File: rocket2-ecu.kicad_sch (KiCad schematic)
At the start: 23 parts, among them J1 ALARM, J24 XT60, P3 PAD_SMD, P4 PAD_SMD, Q1 DMG3402L, U1 BMI088, U2 MS560702BA03-50, U3 BMM150, U4 GC-XPORT-ENH

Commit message: Finished
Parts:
- removed H4: MountingHole_Pad, MountingHole:MountingHole_4.3mm_M4_Pad_Via, symbol Mechanical:MountingHole_Pad
- added R127, R129: 15K, Resistor_SMD:R_0402_1005Metric, symbol Device:R_Small_US
- added R128, R5: 100K, Resistor_SMD:R_0402_1005Metric, symbol Device:R_Small_US
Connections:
- net GND: now also R127.2, R129.2
- net REDs/BATT_IN+ renamed BATT
- net BATT: now also R5.1
- net REDs/GSE_IN+ renamed GSE
- net GSE: now also R128.1
- new net ECU_BV: R127.1, R5.2
- new net ECU_GS: R128.2, R129.1
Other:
- note removed: "FIC GROUND VIAS AND RETURN PATHS"
- note removed: "Reads battery voltage Reads GSE voltage"

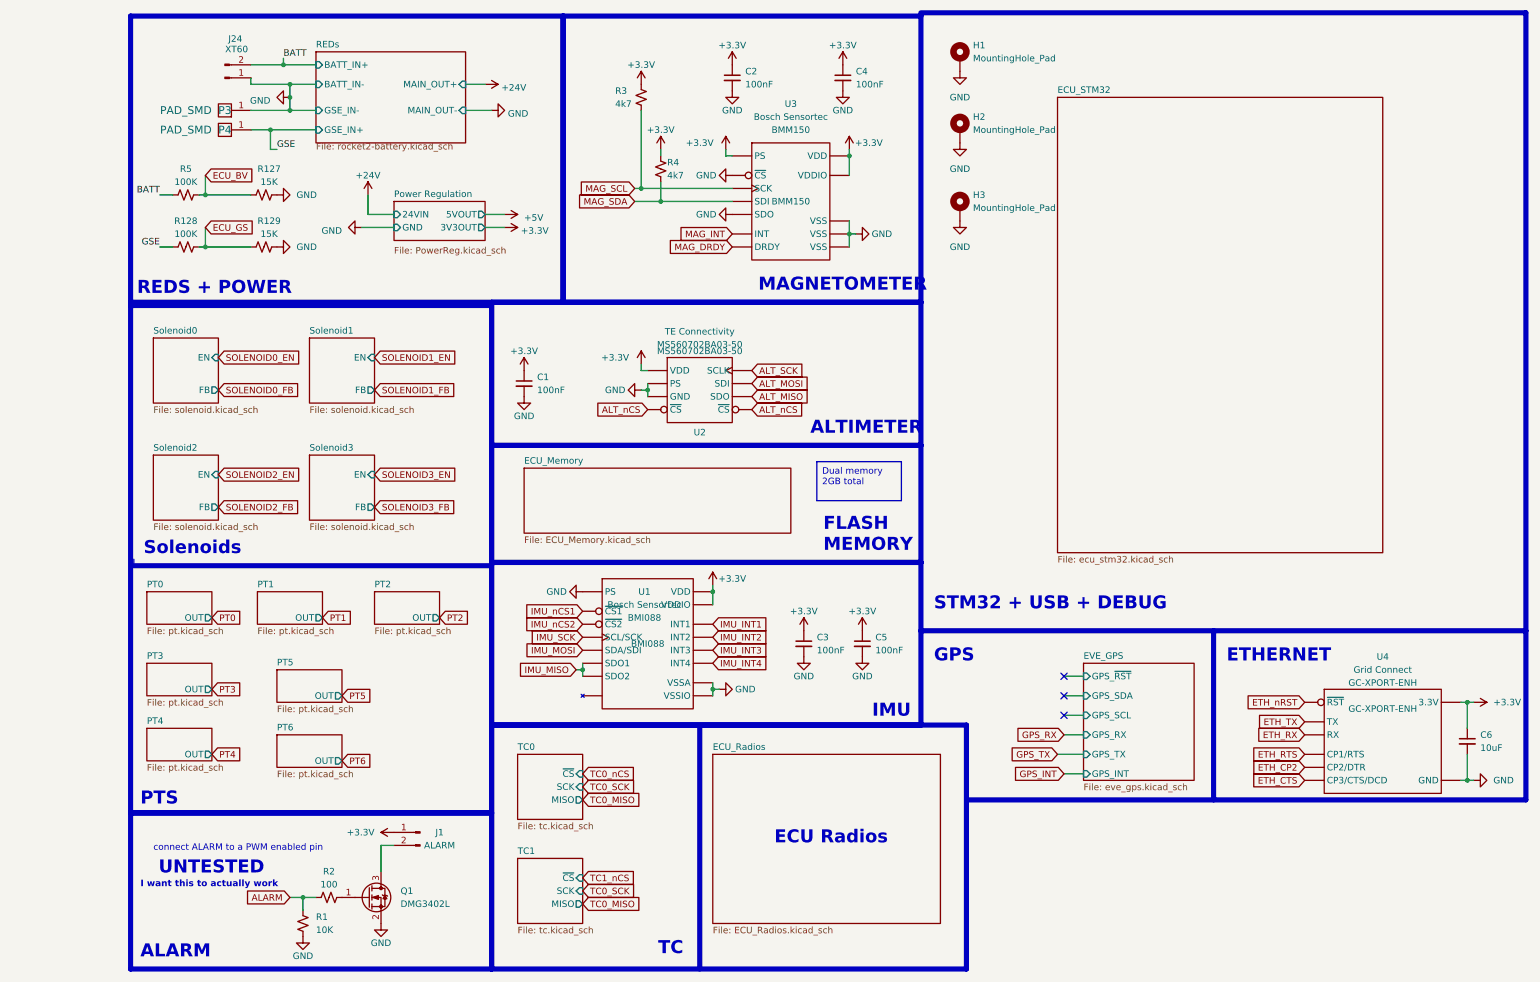
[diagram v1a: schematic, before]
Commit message: REDS updated with diodes and hierarchy to main micro
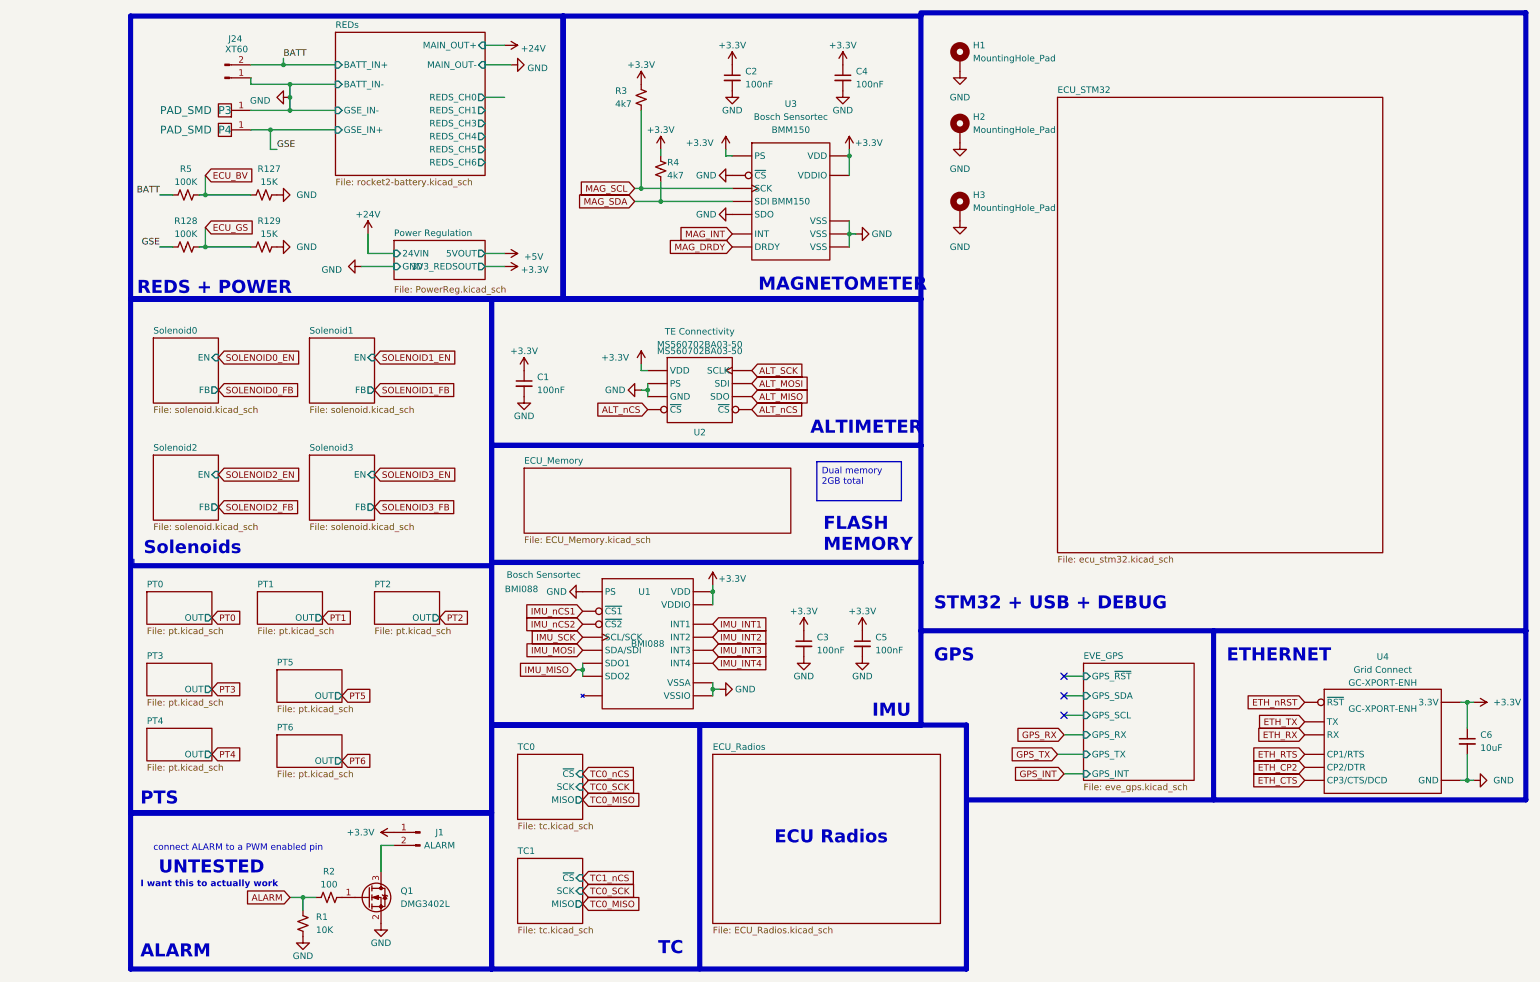
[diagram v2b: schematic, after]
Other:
- sheet Power Regulation ports: added 3V3_REDSOUT; removed 3V3OUT
- sheet REDs ports: added REDS_CH0, REDS_CH1, REDS_CH3, REDS_CH4, REDS_CH5, REDS_CH6; removed none

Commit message: Updated REDS for working
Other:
- sheet REDs ports: added REDS_CH2; removed REDS_CH6
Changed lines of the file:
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@@
 	(wire
 		(pts
+			(xy 81.28 30.48) (xy 82.55 30.48)
+		)
+		(stroke
+			(width 0)
+			(type default)
+		)
+	)
+	(wire
+		(pts
 			(xy 273.05 146.05) (xy 271.78 146.05)
 		)
@@
 	(wire
 		(pts
-			(xy 81.28 27.94) (xy 85.09 27.94)
+			(xy 81.28 27.94) (xy 82.55 27.94)
 		)
 		(stroke
@@
 	(wire
 		(pts
+			(xy 81.28 40.64) (xy 82.55 40.64)
+		)
+		(stroke
+			(width 0)
+			(type default)
+		)
+	)
+	(wire
+		(pts
+			(xy 81.28 33.02) (xy 82.55 33.02)
+		)
+		(stroke
+			(width 0)
+			(type default)
+		)
+	)
+	(wire
+		(pts
 			(xy 193.04 156.21) (xy 198.12 156.21)
 		)
@@
 	(wire
 		(pts
+			(xy 81.28 38.1) (xy 82.55 38.1)
+		)
+		(stroke
+			(width 0)
+			(type default)
+		)
+	)
+	(wire
+		(pts
 			(xy 52.07 25.4) (xy 43.18 25.4)
 		)
@@
 	(wire
 		(pts
+			(xy 81.28 35.56) (xy 82.55 35.56)
+		)
+		(stroke
+			(width 0)
+			(type default)
+		)
+	)
+	(wire
+		(pts
 			(xy 100.33 139.7) (xy 100.33 140.97)
 		)
@@
 					(size 1.27 1.27)
 				)
+				(hide yes)
 			)
 		)
@@
 			)
 		)
-		(pin "MAIN_OUT-" input
-			(at 81.28 21.59 0)
-			(effects
-				(font
-					(size 1.27 1.27)
-				)
-				(justify right)
-			)
-		)
-		(pin "MAIN_OUT+" input
-			(at 81.28 17.78 0)
-			(effects
-				(font
-					(size 1.27 1.27)
-				)
-				(justify right)
-			)
-		)
 		(pin "BATT_IN-" input
 			(at 52.07 25.4 180)
@@
 		)
 		(pin "REDS_CH4" output
-			(at 81.28 35.56 0)
+			(at 81.28 38.1 0)
 			(effects
 				(font
@@
 		)
 		(pin "REDS_CH3" output
-			(at 81.28 33.02 0)
+			(at 81.28 35.56 0)
 			(effects
 				(font
@@
 		)
 		(pin "REDS_CH5" output
-			(at 81.28 38.1 0)
+			(at 81.28 40.64 0)
 			(effects
 				(font
@@
 			)
 		)
-		(pin "REDS_CH6" output
-			(at 81.28 40.64 0)
+		(pin "REDS_CH2" output
+			(at 81.28 33.02 0)
+			(effects
+				(font
+					(size 1.27 1.27)
+				)
+				(justify right)
+			)
+		)
+		(pin "MAIN_OUT-" input
+			(at 81.28 21.59 0)
+			(effects
+				(font
+					(size 1.27 1.27)
+				)
+				(justify right)
+			)
+		)
+		(pin "MAIN_OUT+" input
+			(at 81.28 17.78 0)
 			(effects
 				(font

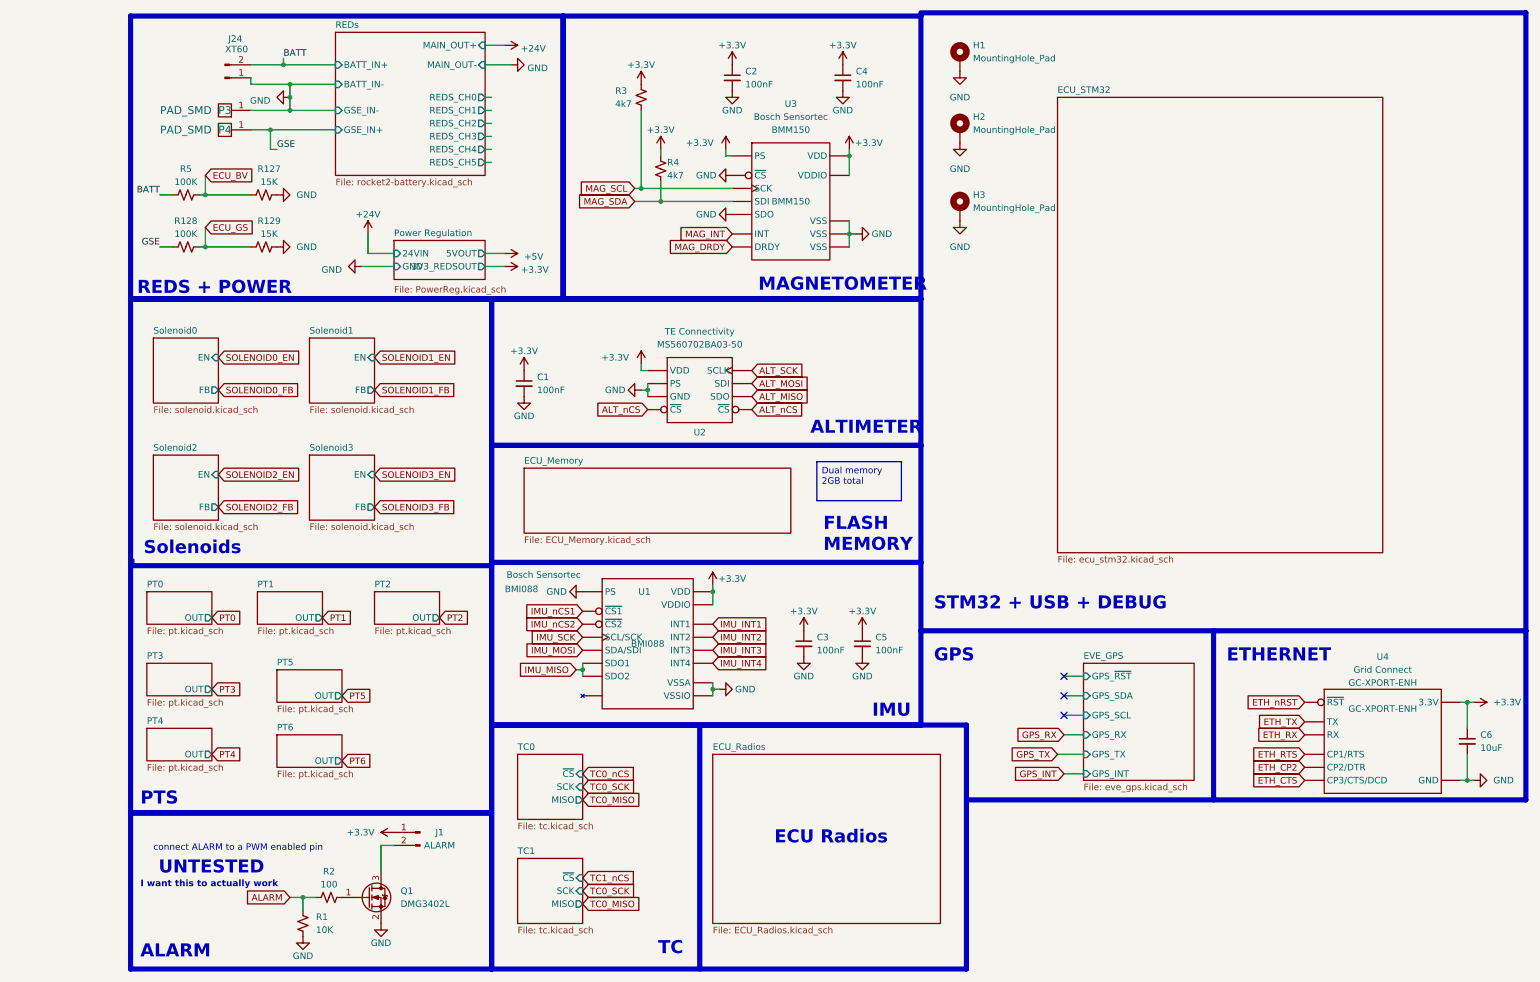
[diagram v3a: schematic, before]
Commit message: Added power sense to rocket2-battery with voltage follower, added +1 solenoids and PT circuit, made new gx connectors
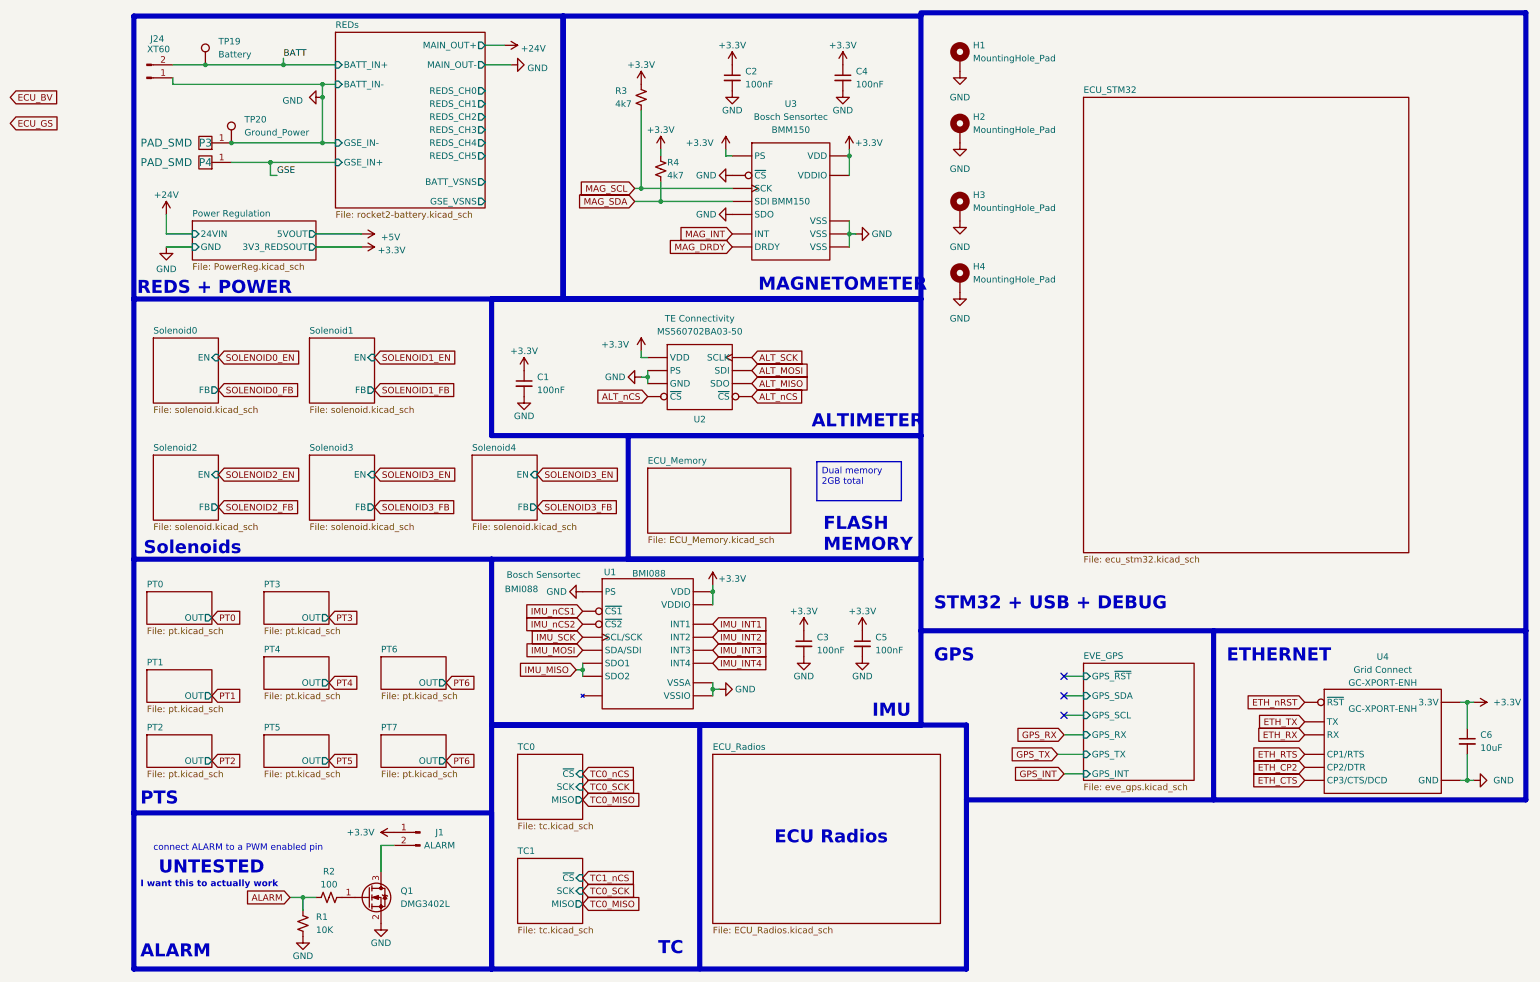
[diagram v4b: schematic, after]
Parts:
- removed R127, R129: 15K, Resistor_SMD:R_0402_1005Metric, symbol Device:R_Small_US
- removed R128, R5: 100K, Resistor_SMD:R_0402_1005Metric, symbol Device:R_Small_US
- added H4: MountingHole_Pad, MountingHole:MountingHole_4.3mm_M4_Pad_Via, symbol Mechanical:MountingHole_Pad
- added TP19: Battery, TestPoint:TestPoint_Plated_Hole_D2.0mm, symbol Connector:TestPoint
- added TP20: Ground_Power, TestPoint:TestPoint_Plated_Hole_D2.0mm, symbol Connector:TestPoint
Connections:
- net BATT: now also TP19.1
- net GND: now also H4.1, TP20.1
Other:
- added sheet PT7 (pt.kicad_sch)
- added sheet Solenoid4 (solenoid.kicad_sch)
- sheet REDs ports: added BATT_VSNS, GSE_VSNS; removed none
- moved on the sheet: J24, P3, P4, U2

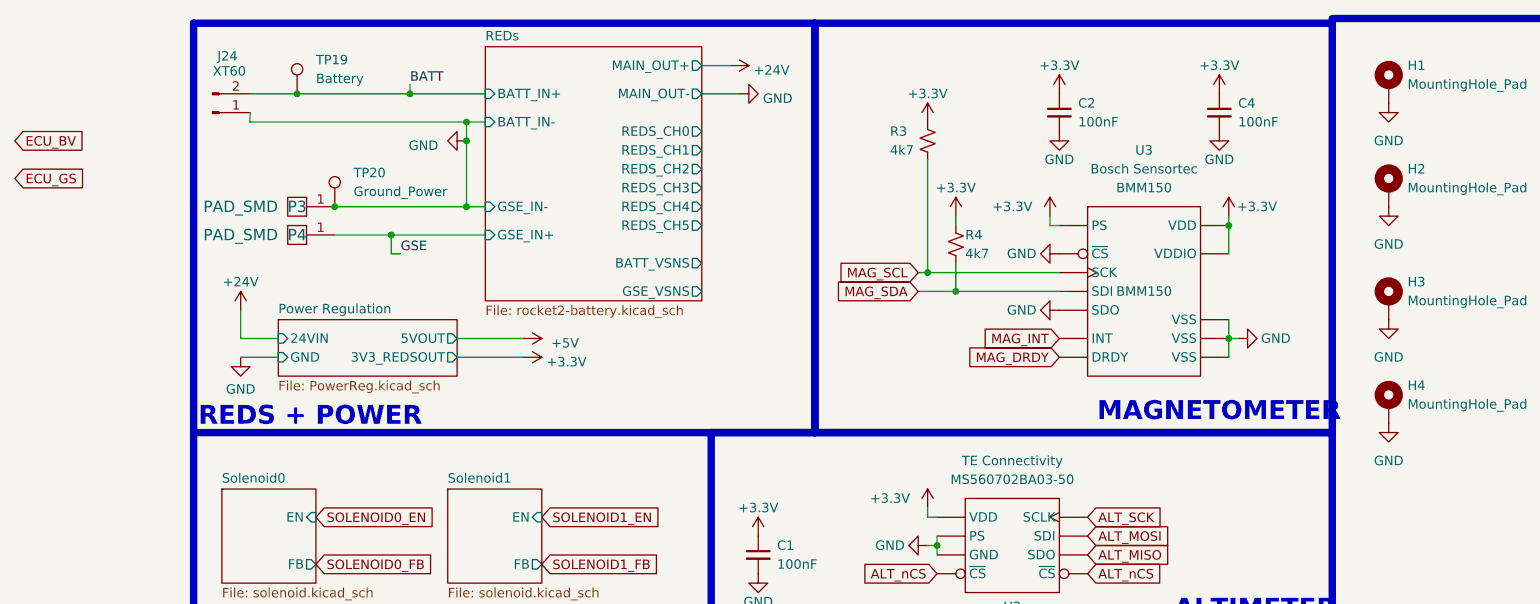
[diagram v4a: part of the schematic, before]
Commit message: moved from bmm150 to bmm350
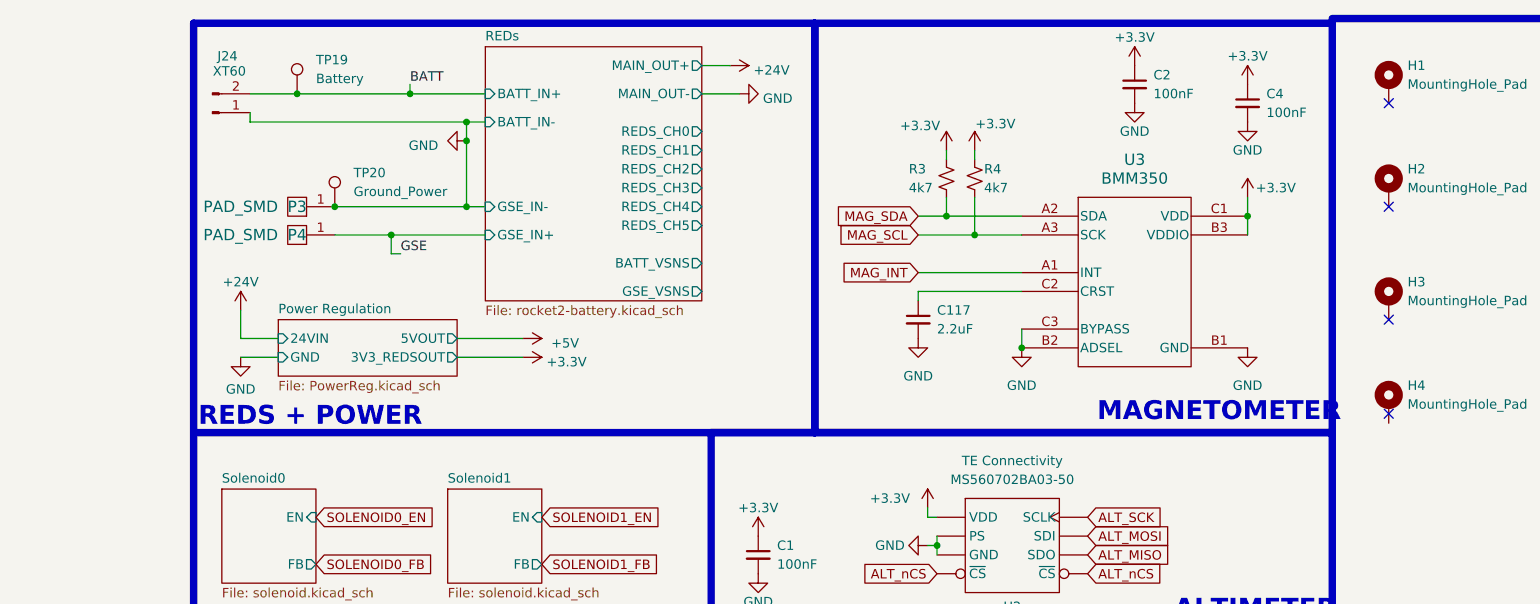
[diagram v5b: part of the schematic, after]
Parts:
- removed U3: BMM150, Package_CSP:WLCSP-12_1.56x1.56mm_P0.4mm, symbol UCIRP-KiCAD-Lib:BMM150
- added C117: 2.2uF, Capacitor_SMD:C_0402_1005Metric, symbol Device:C_Small
- added U3: BMM350, 0UCIRP-KiCAD-Lib:BMM350, symbol 0UCIRP-KiCAD-Lib:BMM350
- J1: footprint 0UCIRP-KiCAD-Lib:CMI-0955-03TH_Buzzer -> Buzzer_Beeper:Buzzer_TDK_PS1240P02BT_D12.2mm_H6.5mm
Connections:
- net +3.3V: now also U3.B3 (VDDIO), U3.C1 (VDD)
- net GND: now also C117.2, U3.B1 (GND), U3.B2 (ADSEL), U3.C3 (BYPASS); no longer H1.1, H2.1, H3.1, H4.1
- net MAG_INT: now also U3.A1 (INT)
- net MAG_SCL: now also R4.2, U3.A3 (SCK); no longer R3.2
- net MAG_SDA: now also R3.2, U3.A2 (SDA); no longer R4.2
- new net: C117.1, U3.C2 (CRST)
- no-connect marks 3 -> 7
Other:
- moved on the sheet: C2, C4, R3, R4
